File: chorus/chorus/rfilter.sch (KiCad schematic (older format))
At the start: 7 parts, among them U6 TL072

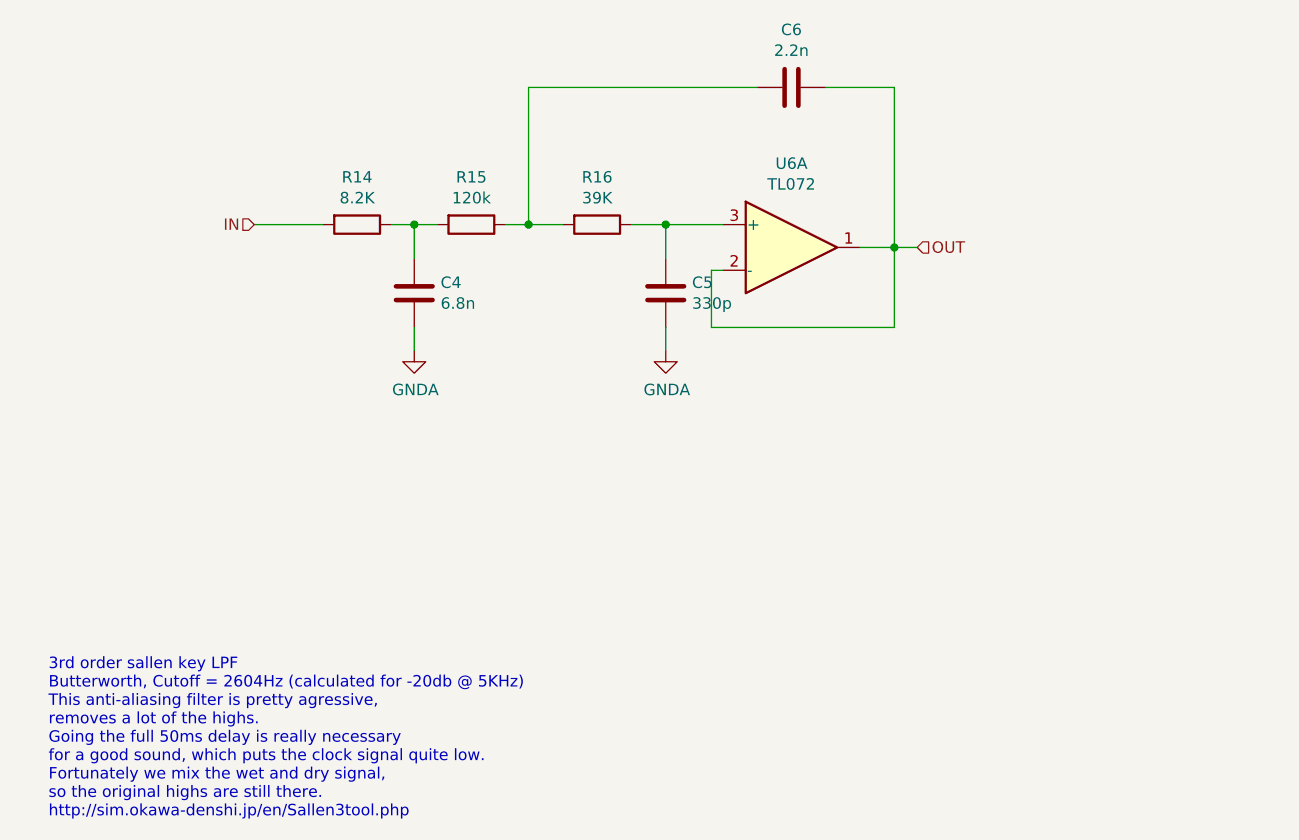
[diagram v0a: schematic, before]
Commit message: add wet/dry mix and recalculate filters
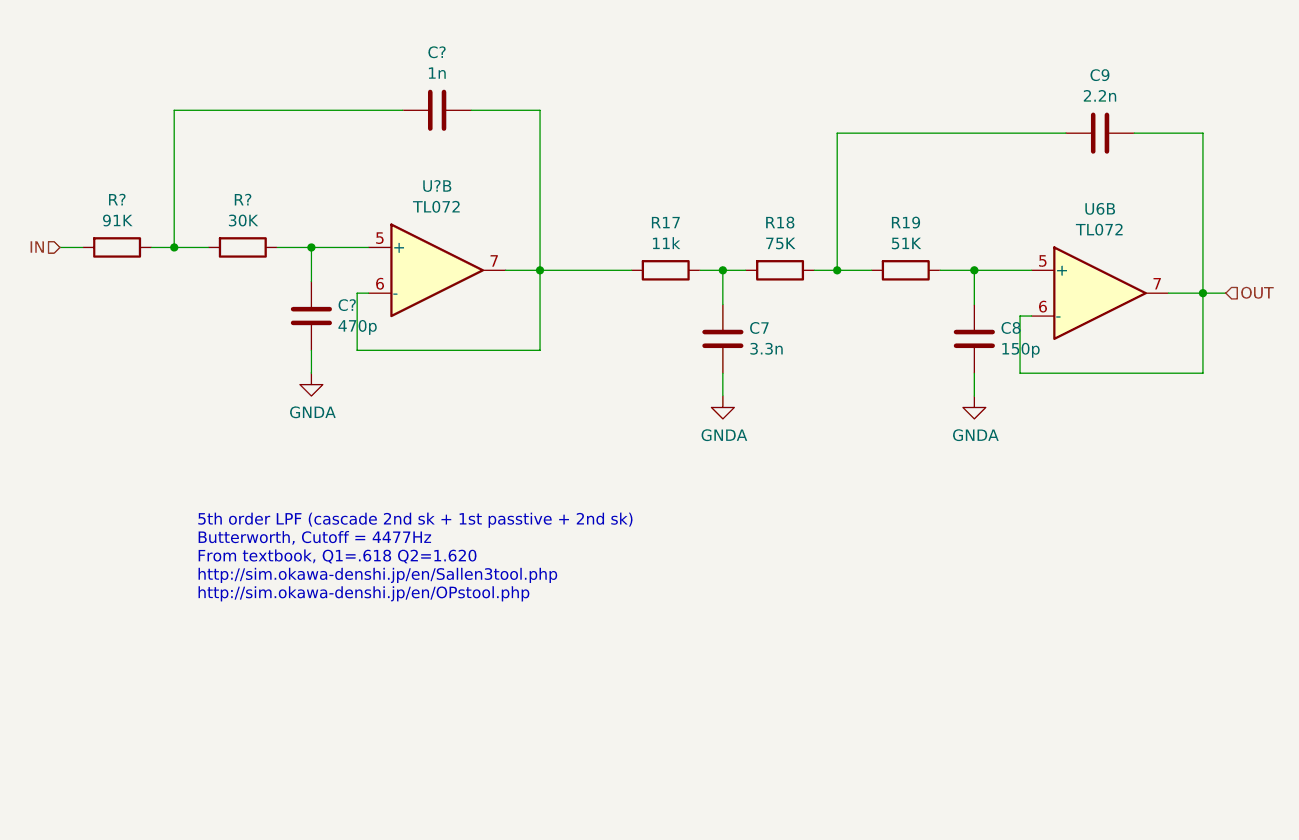
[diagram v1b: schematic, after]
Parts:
- added C?: 1n, Capacitor_THT:C_Disc_D6.0mm_W2.5mm_P5.00mm, symbol Device:C
- added C?: 470p, Capacitor_THT:C_Disc_D6.0mm_W2.5mm_P5.00mm, symbol Device:C
- added R?: 30K, Resistor_THT:R_Axial_DIN0204_L3.6mm_D1.6mm_P2.54mm_Vertical, symbol Device:R
- added R?: 91K, Resistor_THT:R_Axial_DIN0204_L3.6mm_D1.6mm_P2.54mm_Vertical, symbol Device:R
- added U?: TL072, Package_DIP:DIP-8_W7.62mm, symbol Amplifier_Operational:TL072
- C4: value 6.8n -> 3.3n
- C5: value 330p -> 150p
- R14: value 8.2K -> 11k
- R15: value 120k -> 75K
- R16: value 39K -> 51K
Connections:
- net GNDA: now also C?.1
- net IN: now also R?.2; no longer R14.2
- net OUT: now also U6.6 (-), U6.7; no longer U6.1, U6.2 (-)
- net at C5.2, R16.1: now also U6.5 (+); no longer U6.3 (+)
- new net: C?.1, R14.2, U?.6 (-), U?.7
- new net: C?.2, R?.1, U?.5 (+)
- new net: C?.2, R?.1, R?.2
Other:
- note added: "5th order LPF (cascade 2nd sk + 1st passtive + 2nd sk)\nButterworth, Cutoff = 4477Hz\nFrom textbook, Q1=.618 Q2=1.620\nhttp://sim.okawa-denshi.jp/en/Sallen3tool.php\nhttp://sim.okawa-denshi.jp/en/OPstool.php"
- note removed: "3rd order sallen key LPF\nButterworth, Cutoff = 2604Hz (calculated for -20db @ 5KHz)\nThis anti-aliasing filter is pretty agressive,\nremoves a lot of the highs.\nGoing the full 50ms delay is really necessary\nfor a good sound, which puts the clock signal quite low.\nFortunately we mix the wet and dry signal,\nso the original highs are still there.\nhttp://sim.okawa-denshi.jp/en/Sallen3tool.php"
- moved on the sheet: C7, C8, C9, R17, R18, R19
